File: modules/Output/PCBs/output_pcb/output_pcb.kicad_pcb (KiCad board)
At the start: 2 copper layers, 38 x 100 mm, 115 parts, among them J1 THONKICONN, J10 Eurorack_2x5_Power, J11 Conn_01x03_Socket, J2 THONKICONN, J3 ACJS-MV-3, J4 ACJS-MV-3, J5 ACJS-MV-3, U1 TL074, U10 TL074, U11 TL074, U2 TL074, U3 NE5532, U4 NE5532, U5 NE5532, U6 NE5532, U7 TL074, U8 NE5532, U9 NE5532

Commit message: finish output PCB
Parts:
- removed J+6, J+7: Conn_01x07_Pin, Connector_PinHeader_2.54mm:PinHeader_1x07_P2.54mm_Vertical
- removed J+8, J+9: Conn_01x09_Pin, Connector_PinHeader_2.54mm:PinHeader_1x09_P2.54mm_Vertical
- removed J-6, J-7: Conn_01x07_Socket, Connector_PinHeader_2.54mm:PinHeader_1x07_P2.54mm_Vertical
- removed J-8, J-9: Conn_01x09_Socket, Connector_PinHeader_2.54mm:PinHeader_1x09_P2.54mm_Vertical
- removed J10: Eurorack_2x5_Power, Connector_IDC:IDC-Header_2x05_P2.54mm_Vertical
- added B1: Board, kikit:Board, F.Cu at (56.4, 55.2)
- added B2: Board, kikit:Board, F.Cu at (121.3, 59.1)
- added B3: Board, kikit:Board, F.Cu at (184.8, 59.1)
- added C33: 100pF, Capacitor_THT:C_Disc_D4.7mm_W2.5mm_P5.00mm, F.Cu at (207.0, 61.0)
- added C34: 100pF, Capacitor_THT:C_Disc_D4.7mm_W2.5mm_P5.00mm, F.Cu at (186.0, 61.0)
- added D11: GREEN, LED_THT:LED_D3.0mm, F.Cu at (142.2, 141.6)
- added D12: GREEN, LED_THT:LED_D3.0mm, F.Cu at (142.2, 148.0)
- added J12: Conn_01x10_Socket, Connector_PinHeader_2.54mm:PinHeader_1x10_P2.54mm_Vertical, F.Cu at (114.3, 83.8)
- added J13: Conn_01x10_Pin, Connector_PinHeader_2.54mm:PinHeader_1x10_P2.54mm_Vertical, F.Cu at (210.8, 83.8)
- added J21: Conn_01x10_Pin, Connector_PinHeader_2.54mm:PinHeader_1x10_P2.54mm_Vertical, F.Cu at (50.8, 83.8)
- added J22: Conn_01x10_Socket, Connector_PinHeader_2.54mm:PinHeader_1x10_P2.54mm_Vertical, F.Cu at (147.3, 83.8)
- added J23: Conn_01x10_Pin, Connector_PinHeader_2.54mm:PinHeader_1x10_P2.54mm_Vertical, F.Cu at (177.8, 83.8)
- added J6: Eurorack_2x5_Power, Connector_IDC:IDC-Header_2x05_P2.54mm_Vertical, F.Cu at (195.6, 115.6)
- added J7: Conn_01x03_Socket, Connector_PinHeader_2.54mm:PinHeader_1x03_P2.54mm_Vertical, F.Cu at (194.3, 83.2)
- added R46: 10kΩ, Resistor_THT:R_Axial_DIN0207_L6.3mm_D2.5mm_P10.16mm_Horizontal, F.Cu at (147.3, 120.7)
- added R47: 10kΩ, Resistor_THT:R_Axial_DIN0207_L6.3mm_D2.5mm_P10.16mm_Horizontal, F.Cu at (147.3, 134.0)
- added R48: 10kΩ, Resistor_THT:R_Axial_DIN0207_L6.3mm_D2.5mm_P10.16mm_Horizontal, F.Cu at (147.3, 147.3)
- added REF**: logo_small, FreeModualr:logo_small, F.Cu at (206.4, 104.1)
- added U12: TL074, Package_DIP:DIP-14_W7.62mm, F.Cu at (134.6, 78.1)
- C17, C18: value 100pF -> 100nF
- C29, C30: value 10uF -> 100pF; footprint Capacitor_THT:CP_Radial_D4.0mm_P1.50mm -> Capacitor_THT:C_Disc_D4.7mm_W2.5mm_P5.00mm
- C3, C4: value 100pF -> 10uF; footprint Capacitor_THT:C_Disc_D4.7mm_W2.5mm_P5.00mm -> Capacitor_THT:CP_Radial_D4.0mm_P1.50mm
- D7: value RED -> GREEN
- D8: value AMBER -> RED
- D9: value GREEN -> AMBER
- J11: value Conn_01x03_Socket -> Conn_01x10_Pin; footprint Connector_PinHeader_2.54mm:PinHeader_1x03_P2.54mm_Vertical -> Connector_PinHeader_2.54mm:PinHeader_1x10_P2.54mm_Vertical
- R33: value 20kΩ -> 51kΩ
- R34: value 1.3kΩ -> 3k3kΩ
- R35: value 910Ω -> 2k4Ω
- R36: value 2kΩ -> 3k6Ω
- R37: value 270Ω -> 1k3Ω
- R38: value 10kΩ -> 750Ω
- U1: value TL074 -> TL072; footprint Package_DIP:DIP-14_W7.62mm -> Package_DIP:DIP-8_W7.62mm
- moved C18 266.8 mm to (61.5, 57.1), turned to 180 degrees
- moved C17 261.7 mm to (64.1, 69.8), turned to 180 degrees
- moved RV1 202.8 mm to (72.4, 70.4), turned to 90 degrees
- moved R2 200.9 mm to (84.5, 90.8), turned to -90 degrees
- moved RV2 190.5 mm to (59.7, 84.3), turned to 90 degrees
- moved C2 186.3 mm to (81.3, 95.8), turned to 90 degrees
- moved J2 183.5 mm to (74.9, 95.9)
- moved J1 179.6 mm to (59.7, 95.9)
- moved R1 169.1 mm to (50.2, 90.8), turned to -90 degrees
- moved C32 167.5 mm to (122.2, 62.0), turned to -90 degrees
- moved C1 161.2 mm to (53.3, 95.8), turned to 90 degrees
- moved U9 159.8 mm to (180.3, 92.7)
- moved R31 159.5 mm to (118.1, 71.8), turned to -90 degrees
- moved D1 158.4 mm to (118.1, 69.2), turned to 90 degrees
- moved C20 143.2 mm to (187.9, 68.6), turned to 90 degrees
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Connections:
- C1 pad 2: /IO Board/L_IN -> Net-(U1A-+)
- C15 pad 2: GND -> /GND_MAIN
- C16 pad 1: GND -> /GND_MAIN
- C17 pad 1: Net-(U7B--) -> /+12v_FRONT
- C17 pad 2: /Line Level Amp/POT_L_1 -> /GND_FRONT
- C18 pad 1: Net-(U7D--) -> /GND_FRONT
- C18 pad 2: /Line Level Amp/POT_R_1 -> /-12v_FRONT
- C2 pad 2: /IO Board/R_IN -> Net-(U1B-+)
- C25 pad 2: GND -> /GND_MAIN
- C26 pad 1: GND -> /GND_MAIN
- C27 pad 2: GND -> /GND_MAIN
- C28 pad 1: GND -> /GND_MAIN
- C29 pad 1: /+12v_REAR -> Net-(U2A--)
- C29 pad 2: /GND_REAR -> /Headphone Amp/POT_L_1
- C3 pad 1: Net-(U2B--) -> /+12v_REAR
- C3 pad 2: /Headphone Amp/POT_L_1 -> /GND_REAR
- C30 pad 1: /GND_REAR -> Net-(U2D--)
- C30 pad 2: /-12v_REAR -> /Headphone Amp/POT_R_1
- C31 pad 2: GND -> /GND_MAIN
- C32 pad 2: GND -> /GND_MAIN
- C4 pad 1: Net-(U2D--) -> /GND_REAR
- C4 pad 2: /Headphone Amp/POT_R_1 -> /-12v_REAR
- D10 pad 1: GND -> /GND_MAIN
- D3 pad 1: GND -> /GND_MAIN
- D4 pad 1: GND -> /GND_MAIN
- D5 pad 1: GND -> /GND_MAIN
- D6 pad 1: GND -> /GND_MAIN
- D7 pad 1: GND -> /GND_MAIN
- D8 pad 1: GND -> /GND_MAIN
- D9 pad 1: GND -> /GND_MAIN
- J1 pad 1: /IO Board/GND -> /GND_FRONT
- J11 pad 1: GND -> /GND_FRONT
- J11 pad 2: /L_IN -> /+12v_FRONT
- J11 pad 3: /R_IN -> unconnected-(J11-Pin_3-Pad3)
- J2 pad 1: /IO Board/GND -> /GND_FRONT
- J3 pad 1: GND -> /GND_MAIN
- J3 pad 2: (no net) -> unconnected-(J3-Pad2)
- J3 pad 5: (no net) -> unconnected-(J3-Pad5)
- J4 pad 1: GND -> /GND_MAIN
- J4 pad 2: (no net) -> unconnected-(J4-Pad2)
- J4 pad 5: (no net) -> unconnected-(J4-Pad5)
- J5 pad 1: GND -> /GND_MAIN
- J5 pad 2: (no net) -> unconnected-(J5-Pad2)
- J5 pad 5: (no net) -> unconnected-(J5-Pad5)
- R1 pad 1: /IO Board/L_IN -> Net-(U1A-+)
- R1 pad 2: /IO Board/GND -> /GND_FRONT
- R2 pad 1: /IO Board/R_IN -> Net-(U1B-+)
- R2 pad 2: /IO Board/GND -> /GND_FRONT
- R3 pad 1: Net-(U2A--) -> Net-(U2B--)
- R3 pad 2: Net-(U2B--) -> Net-(U2A--)
- R31 pad 2: GND -> /GND_MAIN
- R32 pad 2: GND -> /GND_MAIN
- R36 pad 2: /Volume Meter/-18dbu_REF -> /Volume Meter/-9dbu_REF
- R37 pad 1: /Volume Meter/-18dbu_REF -> /Volume Meter/-9dbu_REF
- R37 pad 2: GND -> /Volume Meter/-18dbu_REF
- R38 pad 1: Net-(R38-Pad1) -> /Volume Meter/-18dbu_REF
- R38 pad 2: Net-(D3-A) -> /GND_MAIN
- R39 pad 2: Net-(D4-A) -> Net-(D3-A)
- R4 pad 1: Net-(U2B--) -> Net-(U2A--)
- R40 pad 2: Net-(D5-A) -> Net-(D4-A)
- R41 pad 2: Net-(D6-A) -> Net-(D5-A)
- R42 pad 2: Net-(D7-A) -> Net-(D6-A)
- R43 pad 2: Net-(D8-A) -> Net-(D7-A)
- R44 pad 2: Net-(D9-A) -> Net-(D8-A)
- R45 pad 2: Net-(D10-A) -> Net-(D9-A)
- R5 pad 2: Net-(U3A--) -> Net-(U3B--)
- R6 pad 1: Net-(U3A--) -> Net-(U3B--)
- R6 pad 2: Net-(U3B-+) -> Net-(U3A-+)
- R7 pad 1: Net-(U3B-+) -> Net-(U3A-+)
- R8 pad 1: Net-(U3B--) -> Net-(U3A--)
- RV1 pad : (no net) -> /GND_FRONT
- RV1 pad 3: /IO Board/HP_POT_L3 -> /IO Board/L_IN
- RV1 pad 6: /IO Board/HP_POT_R3 -> /IO Board/R_IN
- RV2 pad : (no net) -> /GND_FRONT
- RV2 pad 3: /IO Board/HP_POT_L3 -> /IO Board/L_IN
- RV2 pad 6: /IO Board/HP_POT_R3 -> /IO Board/R_IN
- U1 pad 1: /L_IN -> /IO Board/L_IN
- U1 pad 2: /L_IN -> /IO Board/L_IN
- U1 pad 3: Net-(J-6-Pin_2) -> Net-(U1A-+)
- U1 pad 4: /+12v_MAIN -> /-12v_FRONT
- U1 pad 5: Net-(J-7-Pin_2) -> Net-(U1B-+)
- U1 pad 6: /R_IN -> /IO Board/R_IN
- U1 pad 7: /R_IN -> /IO Board/R_IN
- U1 pad 8: Net-(D1-A) -> /+12v_FRONT
- U10 pad 1: Net-(R38-Pad1) -> Net-(R40-Pad1)
- U10 pad 10: /Volume Meter/0dbu_REF -> /Volume Meter/-9dbu_REF
- U10 pad 14: Net-(R41-Pad1) -> Net-(R43-Pad1)
- U10 pad 3: /Volume Meter/+6dbu_REF -> /Volume Meter/+3dbu_REF
- U10 pad 5: /Volume Meter/+3dbu_REF -> /Volume Meter/0dbu_REF
- U10 pad 7: Net-(R39-Pad1) -> Net-(R41-Pad1)
- U10 pad 8: Net-(R40-Pad1) -> Net-(R42-Pad1)
- U11 pad 1: Net-(R42-Pad1) -> Net-(R48-Pad1)
- U11 pad 12: /Volume Meter/-18dbu_REF -> /Volume Meter/+3dbu_REF
- U11 pad 3: /Volume Meter/+6dbu_REF -> /Volume Meter/-18dbu_REF
- U11 pad 5: /Volume Meter/+3dbu_REF -> /Volume Meter/-9dbu_REF
- U11 pad 7: Net-(R43-Pad1) -> Net-(R47-Pad1)
- U11 pad 8: Net-(R44-Pad1) -> Net-(R46-Pad1)
- U2 pad 1: Net-(U2A--) -> /Headphone Amp/POT_L_1
- U2 pad 3: /Headphone Amp/POT_L_2 -> /GND_REAR
- U2 pad 5: /GND_REAR -> /Headphone Amp/POT_L_2
- U2 pad 7: /Headphone Amp/POT_L_1 -> Net-(U2B--)
- U3 pad 1: Net-(U3B-+) -> Net-(U3A--)
- U3 pad 3: /GND_REAR -> Net-(U3A-+)
- U3 pad 5: Net-(U3B-+) -> /GND_REAR
- U3 pad 7: Net-(U3B--) -> Net-(U3A-+)
- U5 pad 3: Net-(U3B-+) -> Net-(U3A-+)
- U5 pad 5: Net-(U3B-+) -> Net-(U3A-+)
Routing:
- net /GND_MAIN: track 0.00 -> 542.9 mm
- net /GND_REAR: track 0.00 -> 329.8 mm
- net /-12v_REAR: track 0.00 -> 193.5 mm
- net /+12v_REAR: track 0.00 -> 175.4 mm
- net /GND_FRONT: track 0.00 -> 139.3 mm
- net /Headphone Amp/POT_R_1: track 0.00 -> 117.2 mm
- net /Headphone Amp/POT_L_1: track 0.00 -> 115.6 mm
- net Net-(J22-Pin_4): track 0.00 -> 91.9 mm
- net /-12v_MAIN: track 0.00 -> 90.9 mm
- net /IO Board/L_IN: track 0.00 -> 88.4 mm
- net /Headphone Amp/POT_L_2: track 0.00 -> 87.8 mm
- net /Headphone Amp/POT_R_2: track 0.00 -> 86.3 mm
- net /HP_OUT_L: track 0.00 -> 83.9 mm
- net Net-(D1-K): track 0.00 -> 82.0 mm
- net Net-(J22-Pin_3): track 0.00 -> 81.8 mm
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- added copper zone on B.Cu, net /GND_FRONT
- added copper zone on F.Cu, net /GND_FRONT
- added copper zone on B.Cu, net /GND_MAIN
- added copper zone on F.Cu, net /GND_MAIN
- added copper zone on B.Cu, net /GND_REAR
- added copper zone on F.Cu, net /GND_REAR
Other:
- board size 38 x 100 mm -> 165 x 103.8 mm
- board text added: "-12v"
- board text added: "Free Modular"
- board text added: "Output back v1.0"
- board text added: "Output front v1.0"
- board text added: "Output middle v1.0"
- board text added: "this machine kills fascists"

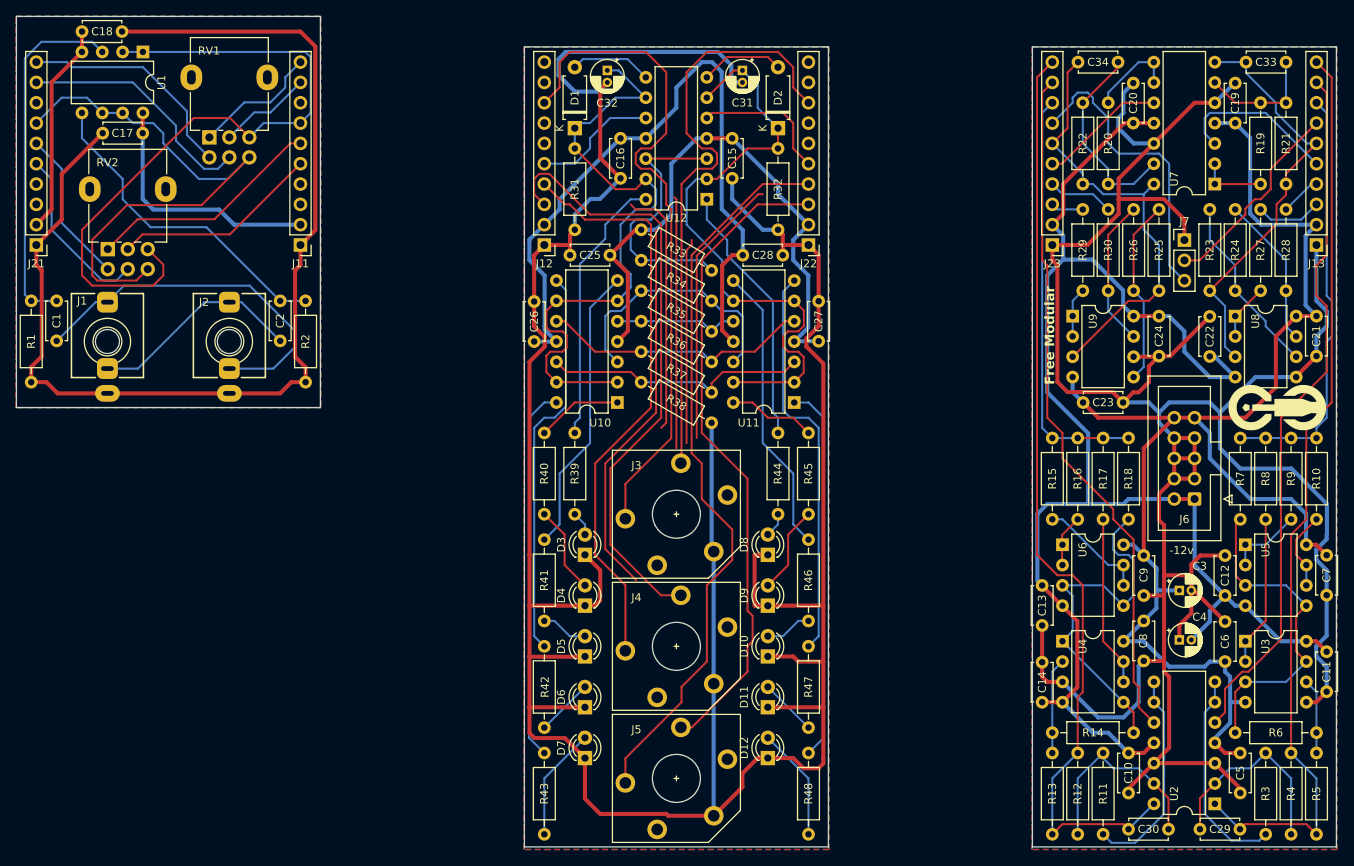
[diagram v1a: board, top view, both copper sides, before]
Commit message: revise output faceplate; add sifam knobs
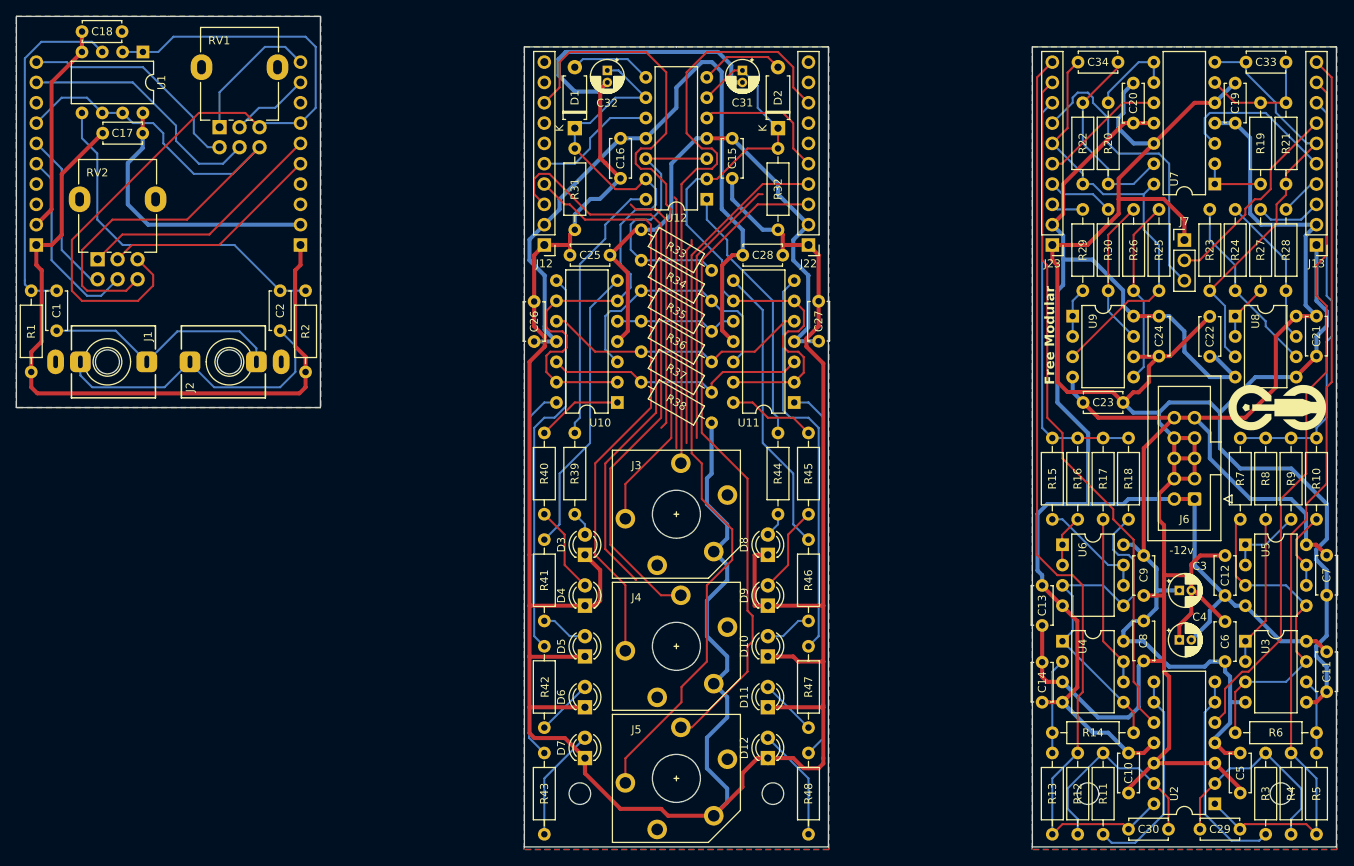
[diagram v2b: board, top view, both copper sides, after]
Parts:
- added H1: MountingHole, MountingHole:MountingHole_2.7mm_M2.5, F.Cu at (142.9, 152.4)
- added H2: MountingHole, MountingHole:MountingHole_2.7mm_M2.5, F.Cu at (118.7, 152.4)
- added H3: MountingHole, MountingHole:MountingHole_2.7mm_M2.5, F.Cu at (182.2, 152.4)
- added H4: MountingHole, MountingHole:MountingHole_2.7mm_M2.5, F.Cu at (206.4, 152.4)
- J11, J21: moved to B.Cu
- moved J1 2.54 mm to (59.7, 98.4), turned to -90 degrees
- moved J2 2.54 mm to (74.9, 98.4), turned to 90 degrees
- moved RV2 1.80 mm to (58.5, 85.6)
- moved RV1 1.80 mm to (73.7, 69.1)
- moved C1 1.27 mm to (53.3, 94.5)
- moved C2 1.27 mm to (81.3, 94.5)
- moved R1 1.27 mm to (50.2, 89.5)
- moved R2 1.27 mm to (84.5, 89.5)
- turned J11 to 0 degrees
- turned J21 to 0 degrees
- renumbered REF** to G1
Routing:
- net /GND_FRONT: track 139.3 -> 91.9 mm
- net Net-(C1-Pad1): track 46.4 -> 30.7 mm
- net Net-(C2-Pad1): track 27.0 -> 38.6 mm
- net /GND_MAIN: track 542.9 -> 549.8 mm
- net /IO Board/L_IN: track 88.4 -> 93.8 mm
- net /IO Board/R_IN: track 70.2 -> 75.0 mm
- net /+12v_FRONT: track 31.8 -> 34.9 mm
- net Net-(U1B-+): track 41.0 -> 43.8 mm
- net /IO Board/LINE_POT_R2: track 21.8 -> 23.8 mm
- net /IO Board/LINE_POT_L1: track 29.6 -> 31.4 mm
- net /IO Board/LINE_POT_L2: track 26.0 -> 27.8 mm
- net /IO Board/HP_POT_L2: track 11.7 -> 9.94 mm
- net /IO Board/HP_POT_L1: track 16.0 -> 17.6 mm
- net Net-(U1A-+): track 44.9 -> 43.6 mm
- net /IO Board/HP_POT_R2: track 30.3 -> 31.6 mm
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
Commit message: tweak silkscreen and alignment
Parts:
- moved C25 0.38 mm to (122.1, 85.1)
- moved C28 0.38 mm to (144.5, 85.1)
- moved U11 0.24 mm to (145.8, 103.5)
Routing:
- net /GND_MAIN: track 549.8 -> 547.0 mm
- net /-12v_MAIN: track 90.9 -> 91.5 mm

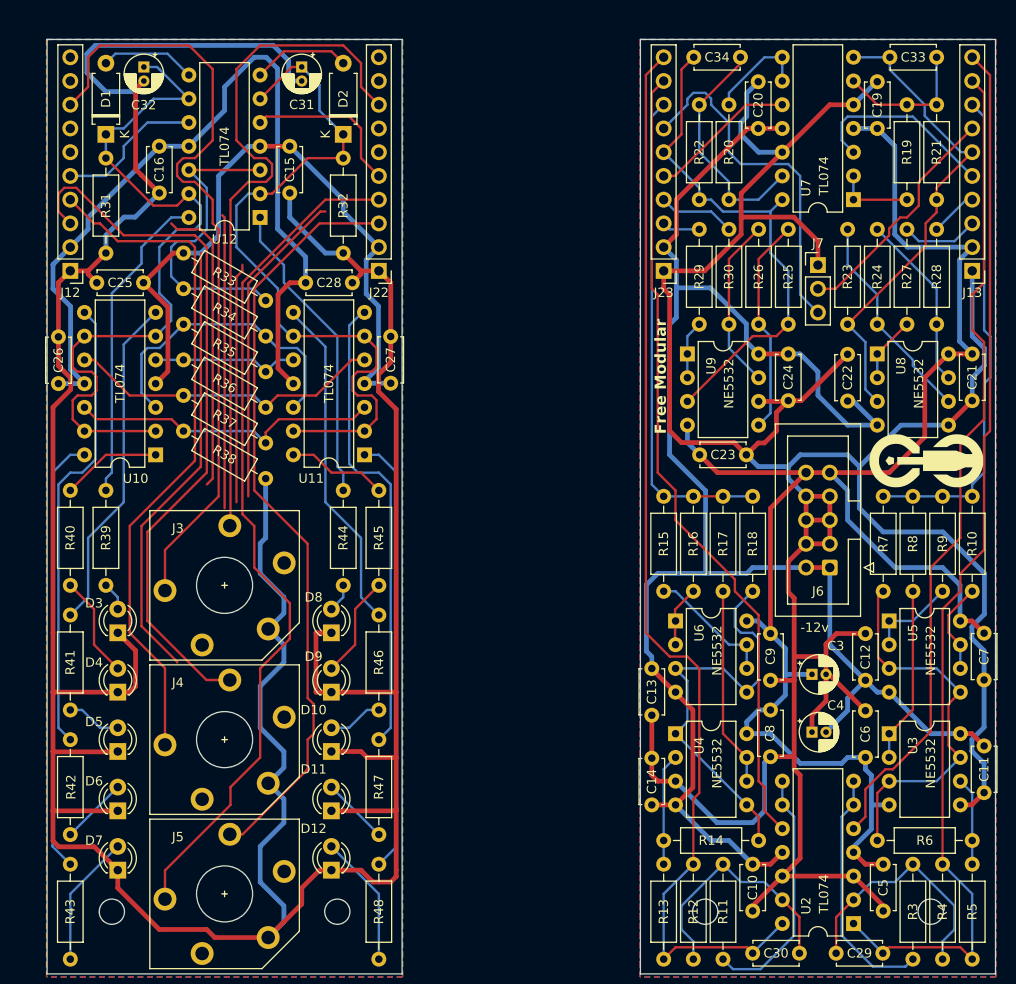
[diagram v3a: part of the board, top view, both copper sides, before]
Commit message: minor tweaks for return path and inductance for output PCB
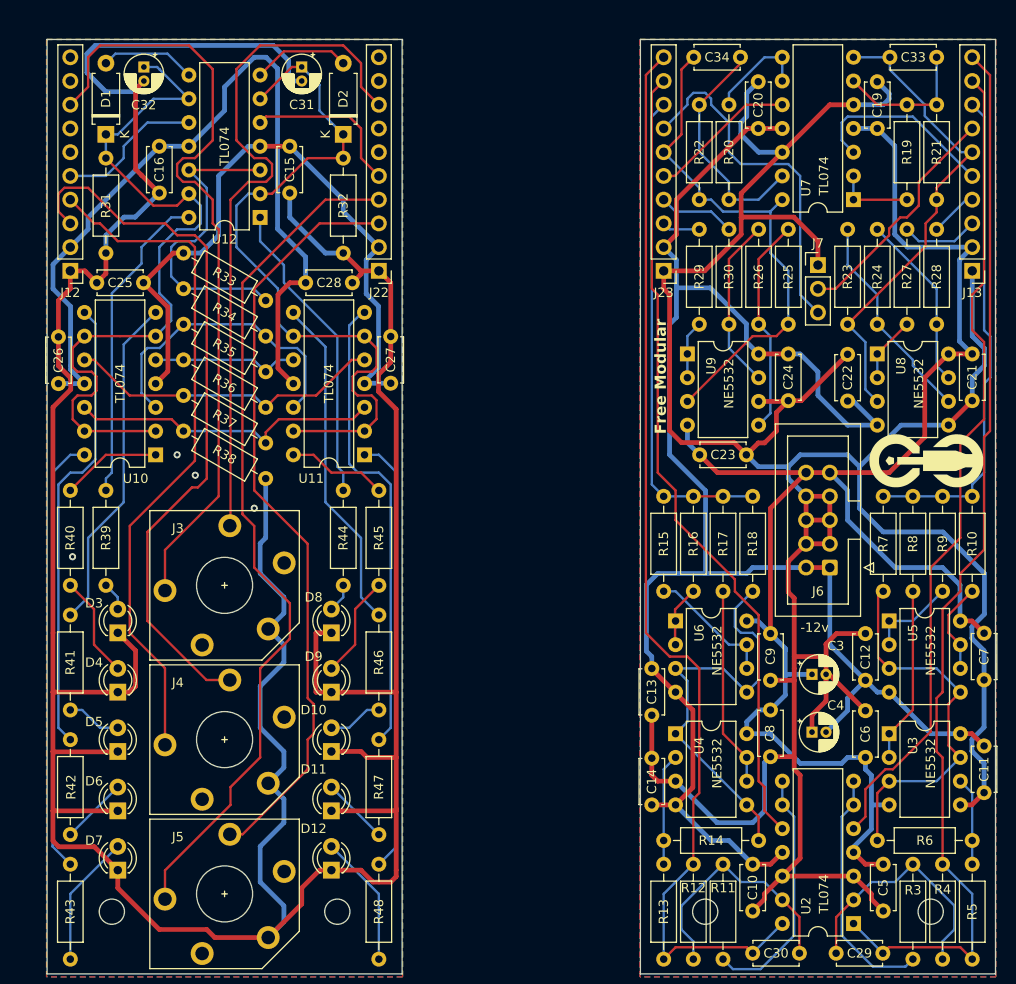
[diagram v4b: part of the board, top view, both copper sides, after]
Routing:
- net /GND_MAIN: track 547.0 -> 376.8 mm, vias 0 -> 4
- net /GND_REAR: track 330.2 -> 334.3 mm
- net /Headphone Amp/POT_L_1: track 115.6 -> 116.1 mm
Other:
- board text added: "Output middle v1.1"
- board text removed: "Output middle v1.0"
